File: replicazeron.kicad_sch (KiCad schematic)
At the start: 74 parts, among them J1 Conn_01x06_Male, J2 Conn_01x06_Male, J3 Conn_01x06_Male, J4 Conn_01x06_Male, J5 Conn_01x06_Male, J6 Conn_01x05_Male, J7 Conn_01x05_Female, J8 Conn_01x06_Female, J9 Conn_01x04_Male, SW1 SW_Push, SW10 SW_Push, SW11 SW_Push, SW12 SW_Push, SW13 SW_Push, SW14 SW_Push, SW15 SW_Push, SW16 SW_Push, SW17 SW_Push, SW18 SW_Push, SW19 SW_Push, SW2 SW_Push, SW20 SW_Push, SW21 SW_Push, SW22 SW_Push, SW23 SW_Push, SW24 SW_Push, SW25 SW_Push, SW26 SW_Push, SW27 SW_Push, SW28 SW_Push, SW29 SW_Push, SW3 SW_Push, SW4 SW_Push, SW5 SW_Push, SW6 SW_Push, SW7 SW_Push, SW8 SW_Push, SW9 SW_Push, U1 STM32F103C8Tx

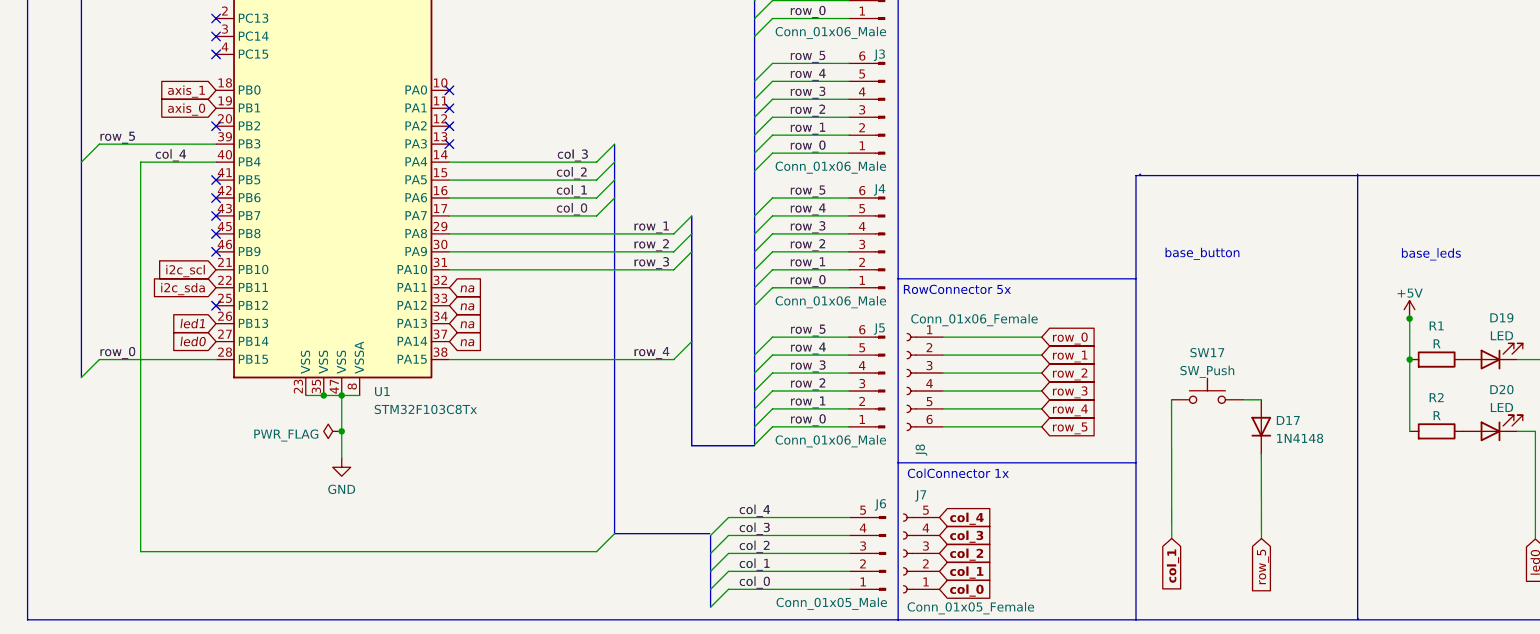
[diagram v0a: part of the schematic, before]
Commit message: update row pin mapping
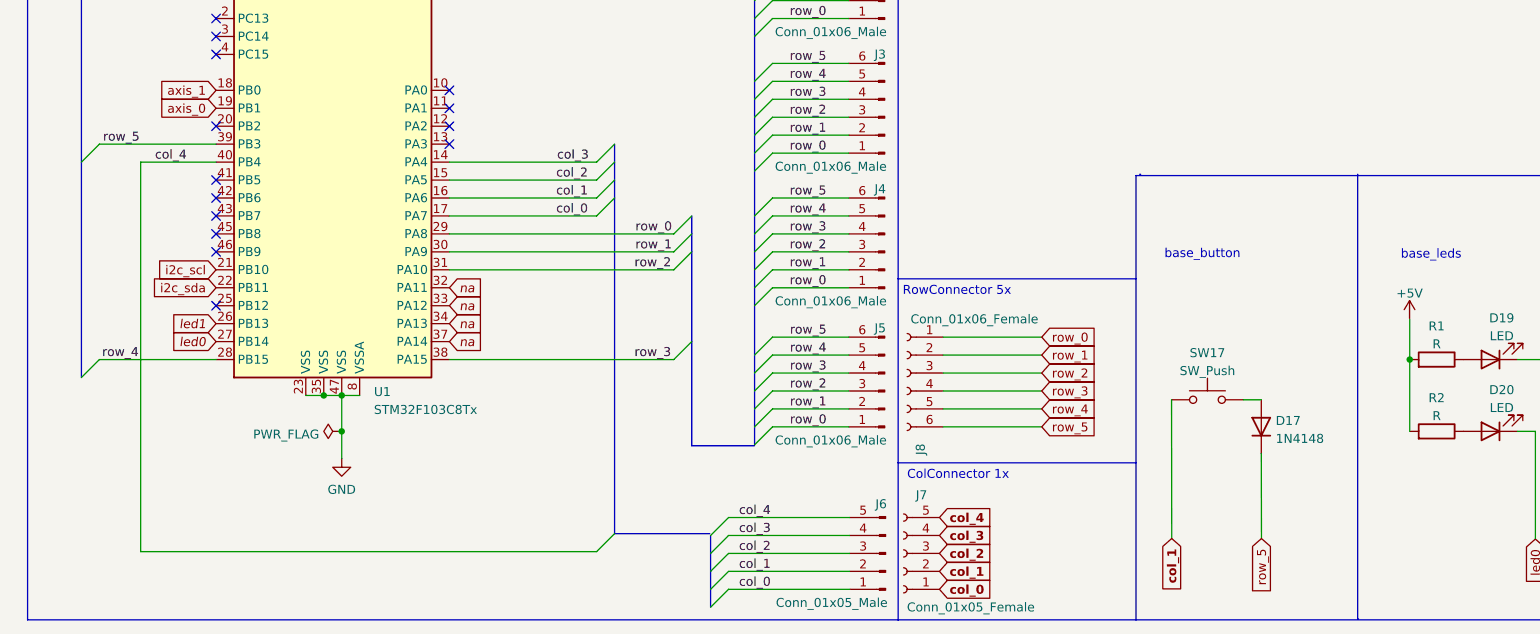
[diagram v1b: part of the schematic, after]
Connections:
- net row_0: now also U1.29 (PA8); no longer U1.28 (PB15)
- net row_1: now also U1.30 (PA9); no longer U1.29 (PA8)
- net row_2: now also U1.31 (PA10); no longer U1.30 (PA9)
- net row_3: now also U1.38 (PA15); no longer U1.31 (PA10)
- net row_4: now also U1.28 (PB15); no longer U1.38 (PA15)

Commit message: set poti vcc to 3v3
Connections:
- net +5V: no longer J9.4 (Pin_4), RV1.1, RV2.1
- new net +3V3: J9.4 (Pin_4), RV1.1, RV2.1

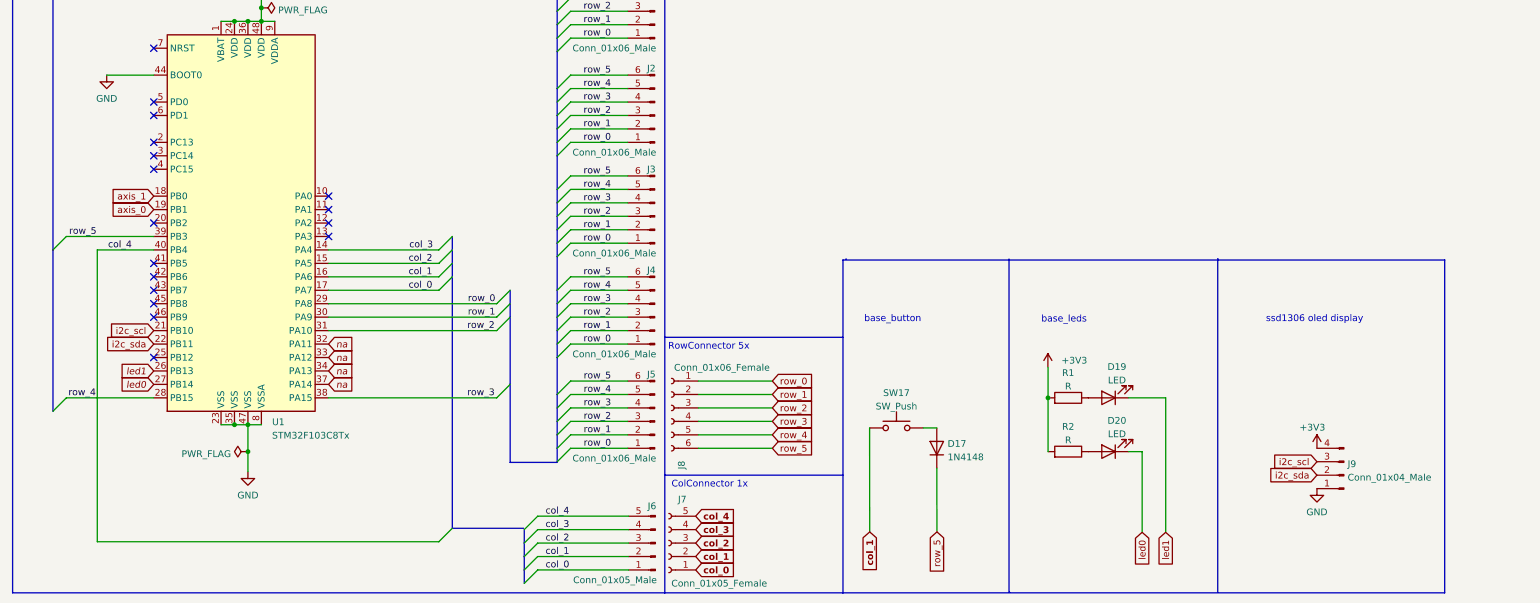
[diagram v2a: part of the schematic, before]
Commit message: add ws2812 to schematics
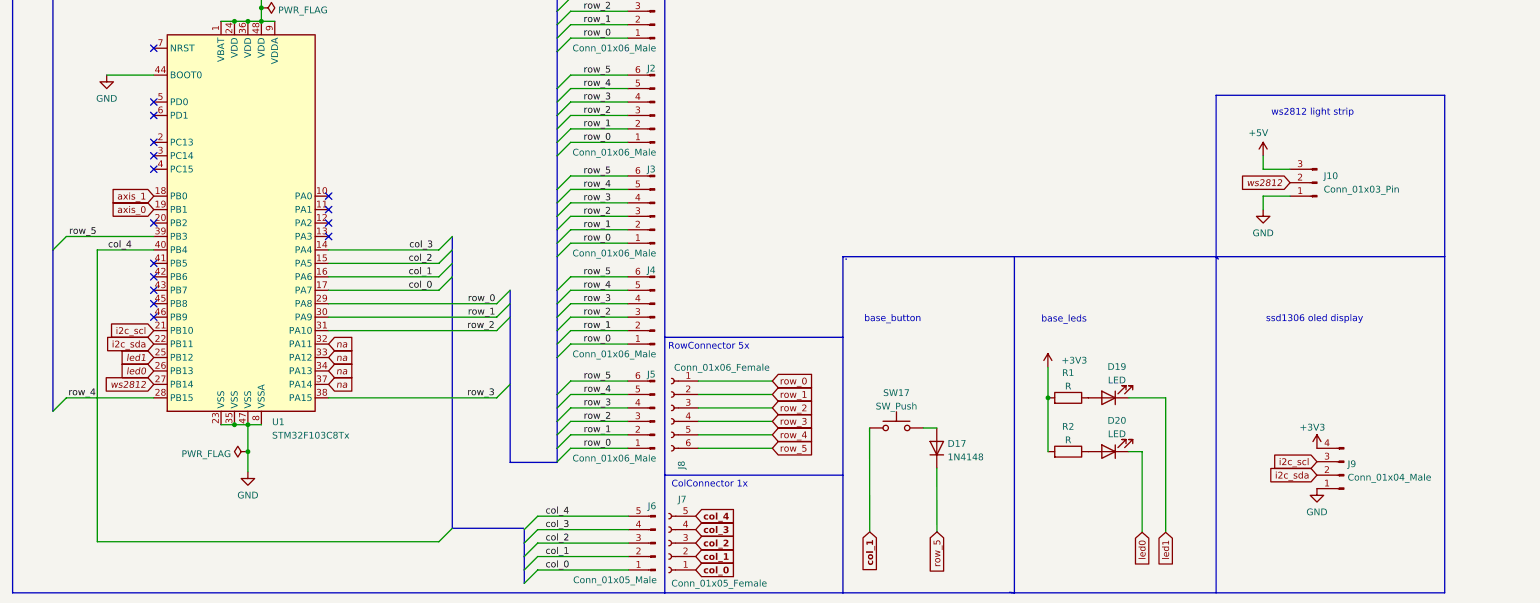
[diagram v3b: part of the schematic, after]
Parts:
- added J10: Conn_01x03_Pin, symbol Connector:Conn_01x03_Pin
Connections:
- net +5V: now also J10.3 (Pin_3)
- net GND: now also J10.1 (Pin_1)
- net led0: now also U1.26 (PB13); no longer U1.27 (PB14)
- net led1: now also U1.25 (PB12); no longer U1.26 (PB13)
- new net ws2812: J10.2 (Pin_2), U1.27 (PB14)
- no-connect marks 17 -> 16
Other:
- note added: "ws2812 light strip"
